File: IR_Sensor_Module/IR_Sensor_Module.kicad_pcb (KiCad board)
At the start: 2 copper layers, 41.5 x 20 mm, 15 parts, among them J1 Conn_01x03, U1 LM393

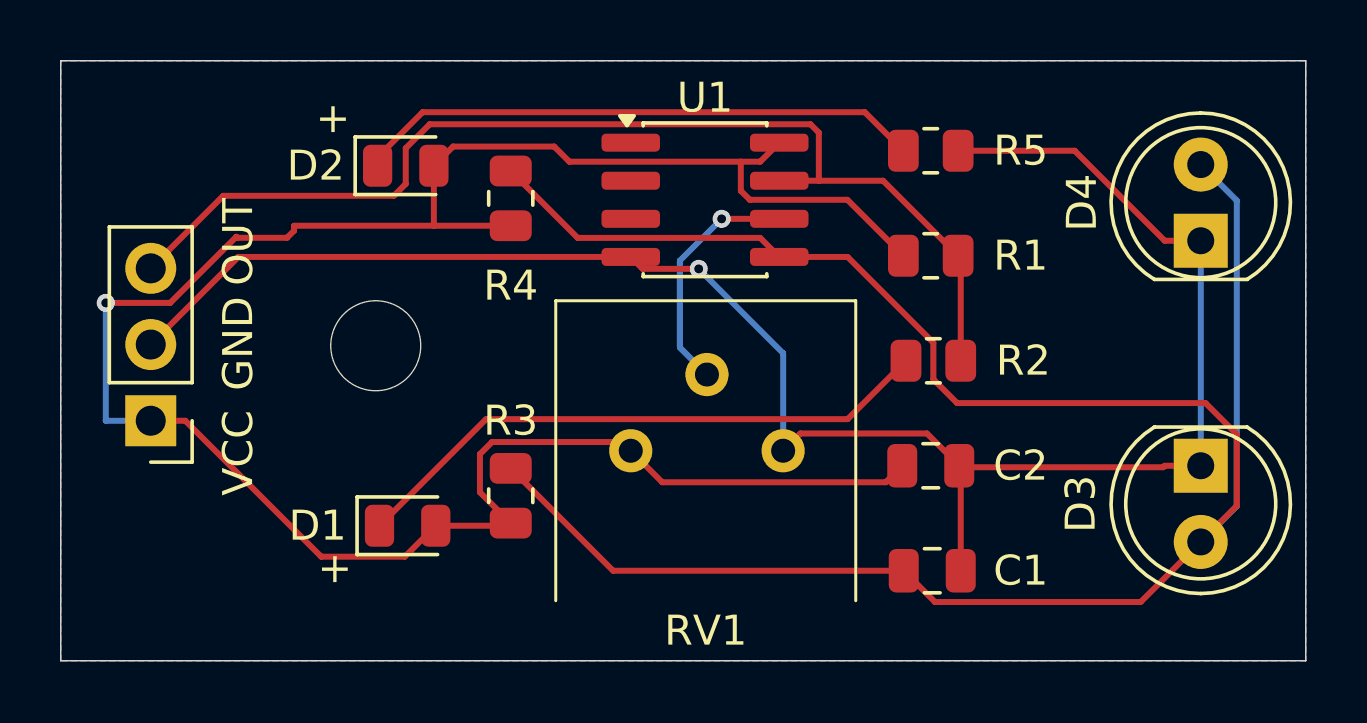
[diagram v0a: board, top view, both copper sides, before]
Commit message: Modified IR Sensor Module
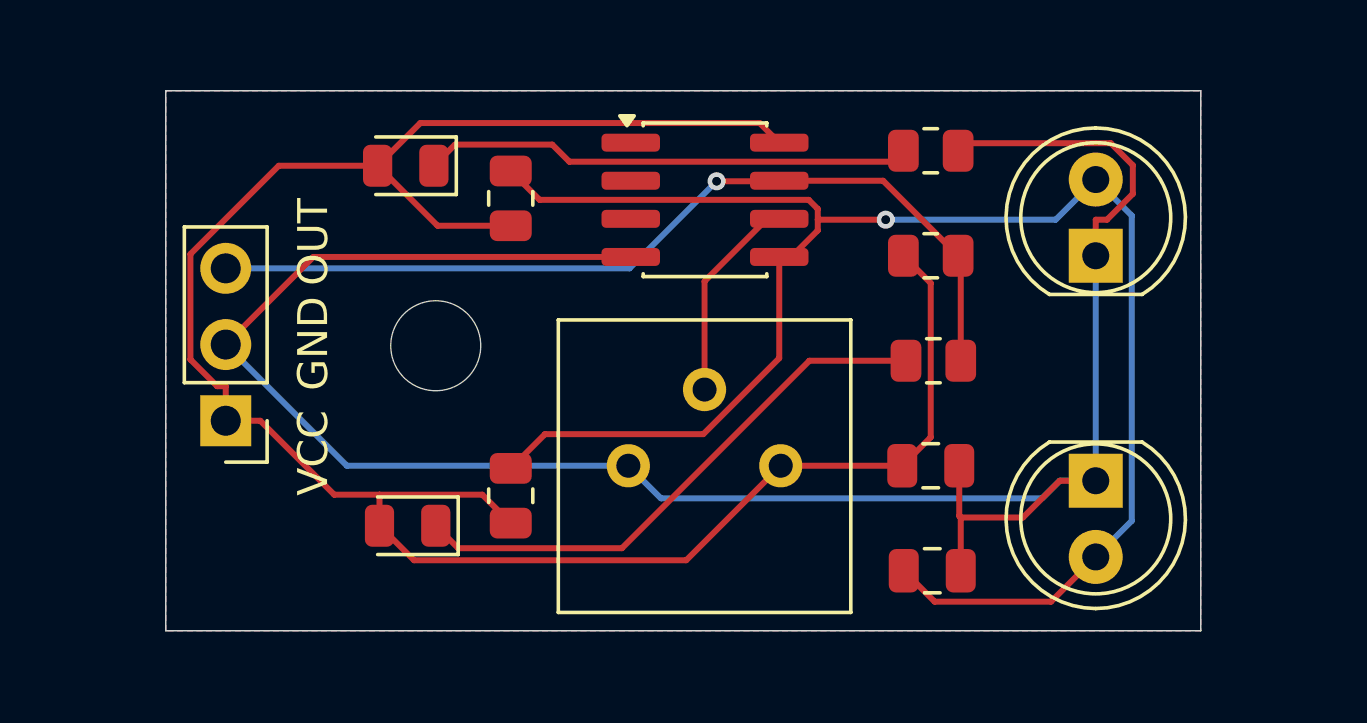
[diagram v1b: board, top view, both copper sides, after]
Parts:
- RV1: moved to F.Cu
- moved RV1 5.02 mm to (105.0, 100.5)
- moved D3 3.54 mm to (115.5, 101.0)
- moved D4 3.54 mm to (115.5, 93.5)
- moved J1 2.50 mm to (86.5, 99.0)
- moved REF** 2.00 mm to (93.5, 96.5)
- turned D1 to 180 degrees
- turned D2 to 180 degrees
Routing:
- net Net-(D3-A): track 71.9 -> 57.8 mm, vias 0 -> 1
- net GND: track 61.8 -> 72.1 mm, vias 1 -> 0
- net /OUT: track 37.2 -> 30.2 mm, vias 0 -> 1
- net Net-(D2-K): track 19.0 -> 16.3 mm
- net VCC: track 73.7 -> 72.1 mm, vias 1 -> 0
- net Net-(D1-K): track 19.8 -> 18.6 mm
- net Net-(U1B--): track 8.06 -> 6.96 mm, vias 1 -> 0
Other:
- board size 41.5 x 20 mm -> 34.5 x 18 mm
- board text added: "RV1"
- board text removed: "+"

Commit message: Modified IR Sensor Module
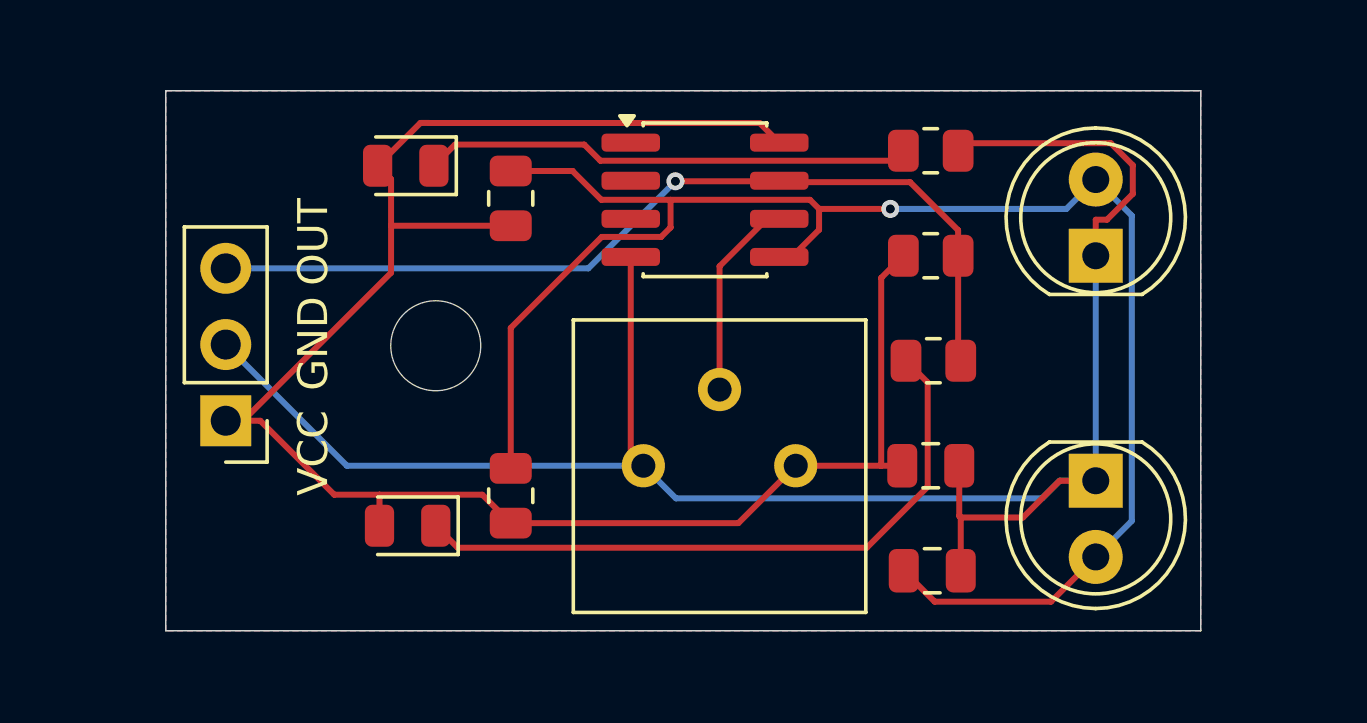
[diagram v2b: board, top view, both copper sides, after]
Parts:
- moved RV1 0.50 mm to (105.5, 100.5)
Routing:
- net VCC: track 72.1 -> 62.1 mm
- net GND: track 72.1 -> 64.5 mm
- net Net-(D1-K): track 18.6 -> 22.0 mm
- net Net-(D3-A): track 57.8 -> 56.2 mm
